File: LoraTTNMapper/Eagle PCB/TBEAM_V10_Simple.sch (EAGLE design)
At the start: 13 parts, among them IC2 ULN2003AD, U1 GY-521MPU6050

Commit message: pcb layout
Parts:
- removed U1: GY-521MPU6050, gy-521:GY-521MPU6050
- added BATTERY_SWITCH: (no value), pinhead:PINHD-1X2
- added BAT_IN, BAT_OUT: (no value), wirepad:SMD5
- added INA219: (no value), pinhead:PINHD-1X6
- added SOLAR_IN: (no value), con-wago-500:W237-102
- added U$2: DC-DC-STEP-DOWN-LM2596, diy-modules:DC-DC-STEP-DOWN-LM2596
- added X1: (no value), con-berg:PN87520
- LED1: value (none) -> Power Rail
- renumbered JP2 to SERVO_2/GPIO32
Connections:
- removed net N$1: U$1.GPIO00, U1.INT
- removed net N$2: IC2.O1, SERVO_1.1, SERVO_2/GPIO32.1
- new net N$10: BATTERY_SWITCH.2, BAT_OUT.P
- new net N$8: U$2.OUT+, X1.1
- new net N$9: BATTERY_SWITCH.1, BAT_IN.P
- new net POWER_RAIL_1_VDD: IC2.O1, IC2.O2, IC2.O3, SERVO_1.1, SERVO_2/GPIO32.1
- new net V_IN_+: INA219.1, SOLAR_IN-1.KL
- new net V_OUT_+: INA219.2, U$2.IN+
- net GND: now also INA219.5, SOLAR_IN-2.KL, U$2.IN-, U$2.OUT-, X1.4; no longer U1.GND
- net GPIO15: now also IC2.I2, IC2.I3
- net SCL: now also INA219.4; no longer U1.SCL
- net SDA: now also INA219.3; no longer U1.SDA
- net VDD: no longer U1.VCC
- net VDD_SWITCHABLE: now also INA219.6
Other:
- note added: "GPIO 4 = Gyro Interrupt"
- note added: "Todo: Servo 2 an Power Rail"
- note removed: "GPIO 0 = Gyro Interrupt"

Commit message: PCB
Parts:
- added GPIO04: FAST LED, pinhead:PINHD-1X3
- added GPIO_BUS: (no value), pinhead:PINHD-1X8
- added I2C, I2C1: (no value), pinhead:PINHD-1X4
- added LED4: VDD Switchable, led:LEDSML1206
- added POWER_RAIL2, V5: (no value), con-wago-500:W237-102
- added R4: 220, resistor:R-EU_R1206
- LED2: value (none) -> GPIO35
- LED3: value (none) -> GPIO32
- R1, R2, R3: value (none) -> 220
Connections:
- removed net POWER_RAIL_1_VDD: IC2.O1, IC2.O2, IC2.O3, SERVO_1.1, SERVO_2/GPIO32.1
- new net GPIO02: GPIO_BUS.5, U$1.GPIO02
- new net GPIO04: GPIO04.1, U$1.GPIO04
- new net GPIO13: GPIO_BUS.4, U$1.GPIO13
- new net GPIO14: GPIO_BUS.3, U$1.GPIO14
- new net GPIO25: GPIO_BUS.2, U$1.GPIO25
- new net GPIO33: GPIO_BUS.1, U$1.GPIO33
- new net GPIO36: IC2.I4, IC2.I5, IC2.I6, IC2.I7, U$1.GPIO36
- new net N$11: LED4.A, R4.1
- new net N$12: IC2.O4, IC2.O5, IC2.O6, IC2.O7, POWER_RAIL2-2.KL
- new net POWER_RAIL_1_GND: GPIO_BUS.6, IC2.O1, IC2.O2, IC2.O3, SERVO_1.1, SERVO_2/GPIO32.1
- net +5V: now also GPIO04.2, IC2.CD+, POWER_RAIL2-1.KL, SERVO_1.2, SERVO_2/GPIO32.2
- net GND: now also GPIO04.3, GPIO_BUS.7, I2C.3, I2C1.3, LED4.C, V5-1.KL
- net N$8: now also V5-2.KL
- net SCL: now also I2C.2, I2C1.2, U$1.SDA; no longer U$1.SCL
- net SDA: now also I2C.1, I2C1.1, U$1.SCL; no longer U$1.SDA
- net VDD: now also GPIO_BUS.8; no longer IC2.CD+, SERVO_1.2, SERVO_2/GPIO32.2
- net VDD_SWITCHABLE: now also I2C.4, I2C1.4, R4.2
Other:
- note added: "GPIO04 FAST Led GPIO15 Servo Power Rail GPIO36 Servo Power Rail 2 GPIO35 Servo 1 Signal GPIO32 Servo 2 Signal"
- note removed: "GPIO 4 = Gyro Interrupt"
- note removed: "GPIO15 Servo Power Rail GPIO35 Servo 1 Signal GPIO32 Servo 2 Signal"

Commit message: updates
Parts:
- added LED5, LED6, LED7, LED8, LED9: Power Rail, led:LEDSML1206
- added R5, R6, R7, R8, R9: 470, resistor:R-EU_R0603
- R1, R2, R3, R4: value 220 -> 470; device resistor:R-EU_R1206 -> resistor:R-EU_R0603
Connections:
- new net GPIO39: GPIO_BUS.1, R5.2, U$1.GPIO39
- new net N$13: LED5.A, R5.1
- new net N$14: U$1.RST
- new net N$15: LED6.A, R6.1
- new net N$16: LED7.A, R7.1
- new net N$17: LED8.A, R8.1
- new net N$18: LED9.A, R9.2
- net GND: now also LED5.C, LED6.C, LED7.C, LED8.C, LED9.C
- net GPIO02: now also GPIO04.1, R8.2
- net GPIO04: now also R3.2, SERVO_2/GPIO32.3; no longer GPIO04.1
- net GPIO13: now also R2.2, SERVO_1.3
- net GPIO14: now also R7.2
- net GPIO25: now also R6.2
- net GPIO32: no longer R3.2, SERVO_2/GPIO32.3
- net GPIO33: no longer GPIO_BUS.1
- net GPIO35: no longer R2.2, SERVO_1.3
- net GPIO36: now also R9.1
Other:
- note added: "GPIO04 FAST Led GPIO15 Servo Power Rail GPIO36 Servo Power Rail 2 GPIO13 Servo 1 Signal GPIO04 Servo 2 Signal"
- note removed: "GPIO04 FAST Led GPIO15 Servo Power Rail GPIO36 Servo Power Rail 2 GPIO35 Servo 1 Signal GPIO32 Servo 2 Signal"

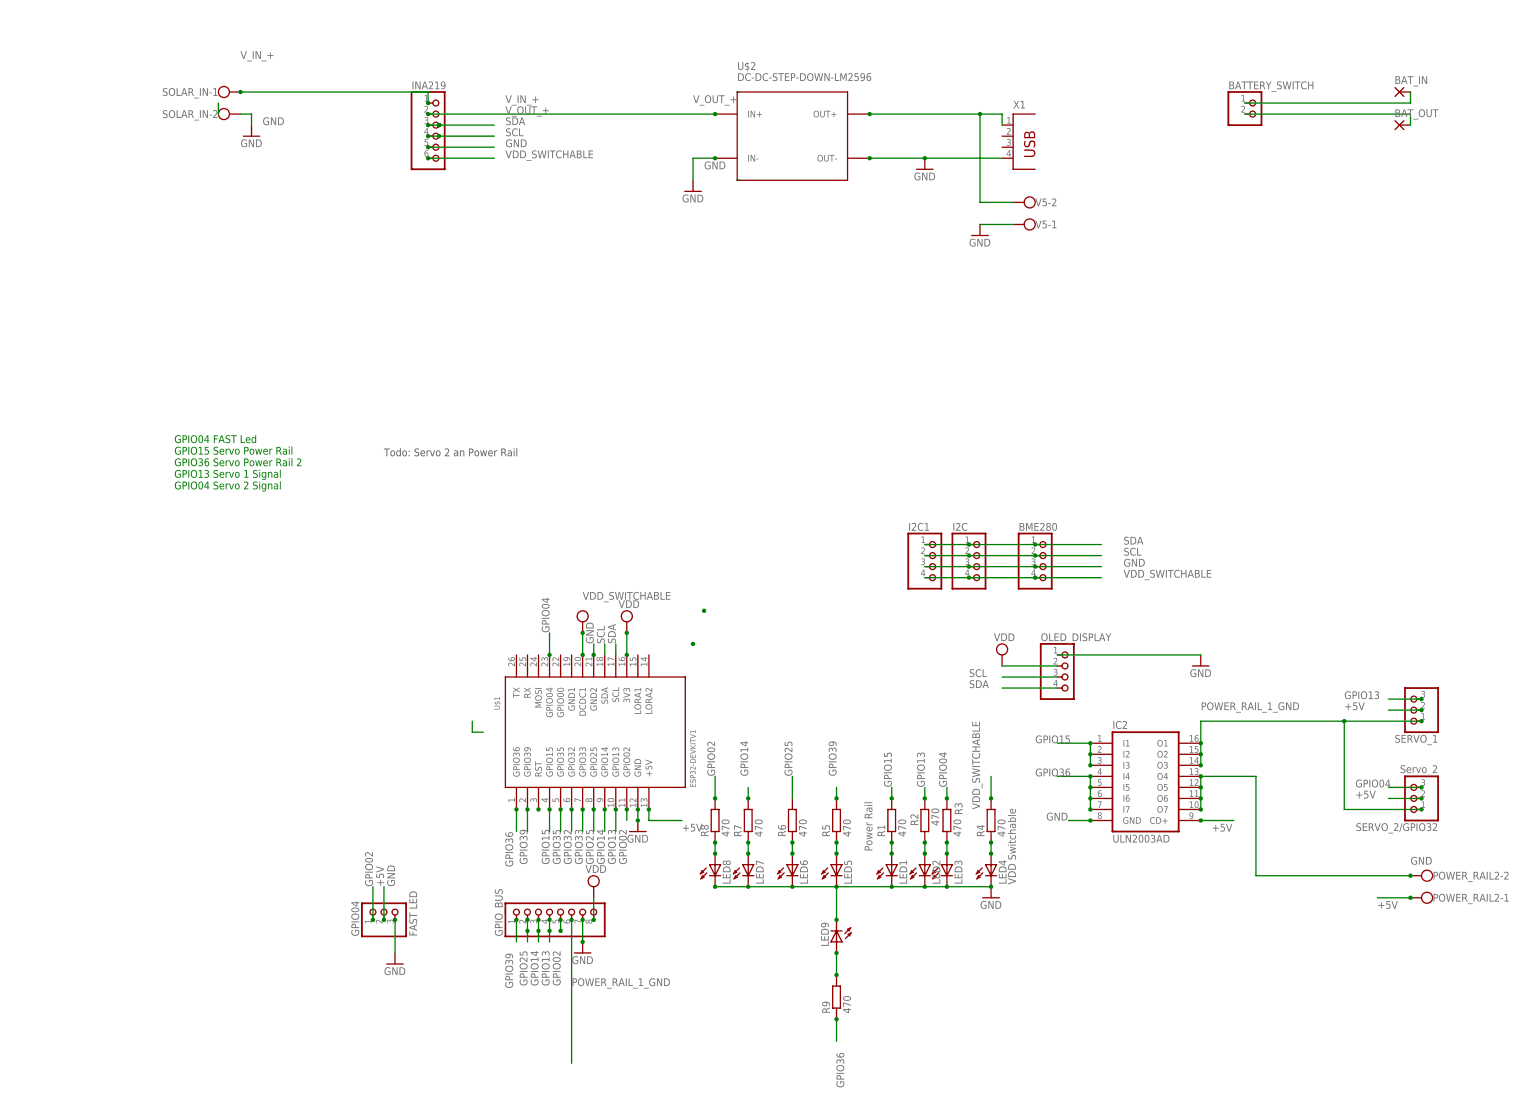
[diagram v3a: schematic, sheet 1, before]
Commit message: PCB Update P Mosfet to switch Solar Panel
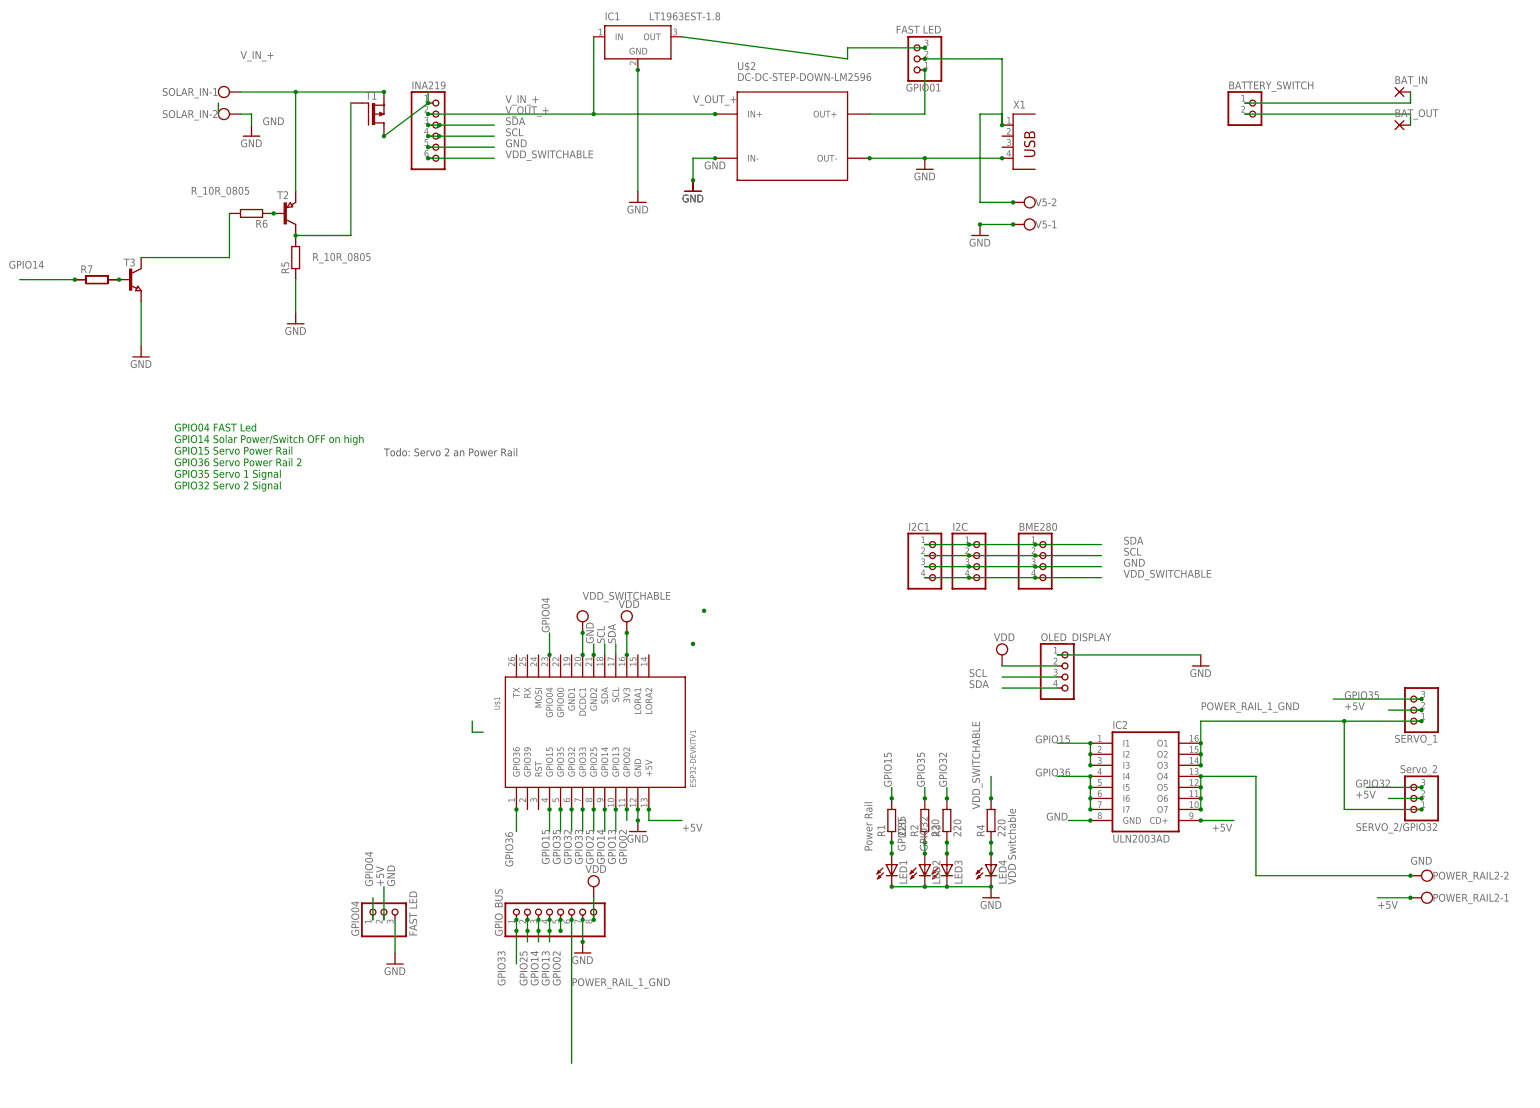
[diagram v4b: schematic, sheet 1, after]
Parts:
- removed LED5, LED6, LED7, LED8, LED9: Power Rail, led:LEDSML1206
- removed R9: 470, resistor:R-EU_R0603
- added GPIO01: FAST LED, pinhead:PINHD-1X3
- added IC1: LT1963EST-1.8, linear-technology:LT1963EST-1.8
- added T1: T_P-MOSFET_AO3401A_ALPHA_SOT23-GSD, JLC PCB Basic Parts_loc:T_P-MOSFET_AO3401A_ALPHA_SOT23-GSD
- added T2: T_PNP_SS8550-Y2_CHANGJ_SOT23-BEC, JLC PCB Basic Parts_loc:T_PNP_SS8550-Y2_CHANGJ_SOT23-BEC
- added T3: T_NPN_SS8050_CHANGJ_SOT23-BEC, JLC PCB Basic Parts_loc:T_NPN_SS8050_CHANGJ_SOT23-BEC
- R1, R2, R3, R4: value 470 -> 220; device resistor:R-EU_R0603 -> resistor:R-EU_R1206
- R5, R6: value 470 -> R_10R_0805; device resistor:R-EU_R0603 -> JLC PCB Basic Parts_loc:R_10R_0805
- R7, R8: value 470 -> R_1.8K_0805; device resistor:R-EU_R0603 -> JLC PCB Basic Parts_loc:R_1.8K_0805
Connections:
- removed net GPIO39: GPIO_BUS.1, R5.2, U$1.GPIO39
- new net BUCK-CONVERTER: GPIO01.1, U$2.OUT+
- net GND: now also IC1G$1.GND, R5.1, T3.E; no longer LED5.C, LED6.C, LED7.C, LED8.C, LED9.C
- net GPIO02: no longer GPIO04.1, R8.2
- net GPIO04: now also GPIO04.1; no longer R3.2, SERVO_2/GPIO32.3
- net GPIO13: no longer R2.2, SERVO_1.3
- net GPIO14: now also R7.1, R8.1; no longer R7.2
- net GPIO25: no longer R6.2
- net GPIO32: now also R3.2, SERVO_2/GPIO32.3
- net GPIO33: now also GPIO_BUS.1
- net GPIO35: now also R2.2, SERVO_1.3
- net GPIO36: no longer R9.1
- net N$13: now also SOLAR_IN-1.KL, T1.S, T2.E; no longer LED5.A, R5.1
- net N$14: now also GPIO01.3, IC1G$1.OUT; no longer U$1.RST
- net N$15: now also R5.2, T1.G, T2.C; no longer LED6.A, R6.1
- net N$16: now also R6.1, T2.B; no longer LED7.A, R7.1
- net N$17: now also R6.2, T3.C; no longer LED8.A, R8.1
- net N$18: now also R7.2, R8.2, T3.B; no longer LED9.A, R9.2
- net N$8: now also GPIO01.2; no longer U$2.OUT+
- net V_IN_+: now also T1.D; no longer SOLAR_IN-1.KL
- net V_OUT_+: now also IC1G$1.IN
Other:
- note added: "GPIO04 FAST Led GPIO14 Solar Power/Switch OFF on high GPIO15 Servo Power Rail GPIO36 Servo Power Rail 2 GPIO35 Servo 1 Signal GPIO32 Servo 2 Signal"
- note removed: "GPIO04 FAST Led GPIO15 Servo Power Rail GPIO36 Servo Power Rail 2 GPIO13 Servo 1 Signal GPIO04 Servo 2 Signal"
